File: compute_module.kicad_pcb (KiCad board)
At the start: 4 copper layers, 93.2 x 62.4 mm, 66 parts, among them J1 2001-1-2-21-00-BK, J2 JC-128, P1 POWER, P2 HOST, P3 CAM1, P4 CONN_02X20, Q1 2N7002P.215, Q2 DMP3056L-7, Q3 2N7002P.215, U1 REG1117-3.3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

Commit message: migrate pcb
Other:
- net class Default removed

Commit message: migrate symbols, update footprints
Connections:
- D2 pad 2: Net-(D2-Pad2) -> unconnected-(D2-A-Pad2)
- D3 pad 2: Net-(D3-Pad2) -> unconnected-(D3-A-Pad2)
- D5 pad 3: HDMI_SCL -> Net-(D5-common)
- D6 pad 3: HDMI_SDA -> Net-(D6-common)
- J1 pad 14: Net-(J1-Pad14) -> unconnected-(J1-~-Pad14)
- J2 pad 3: Net-(J2-Pad3) -> unconnected-(J2-TN-Pad3)
- J2 pad 4: Net-(J2-Pad4) -> unconnected-(J2-TR-Pad4)
- MD1 pad 10: Net-(MD1-Pad10) -> unconnected-(MD1G-NC-Pad10)
- MD1 pad 100: Net-(MD1-Pad100) -> unconnected-(MD1E-DSI1_CP-Pad100)
- MD1 pad 101: Net-(MD1-Pad101) -> unconnected-(MD1E-DSI0_DP0-Pad101)
- MD1 pad 102: Net-(MD1-Pad102) -> unconnected-(MD1E-DSI1_CN-Pad102)
- MD1 pad 105: Net-(MD1-Pad105) -> unconnected-(MD1E-DSI0_CN-Pad105)
- MD1 pad 106: Net-(MD1-Pad106) -> unconnected-(MD1E-DSI1_DP3-Pad106)
- MD1 pad 107: Net-(MD1-Pad107) -> unconnected-(MD1E-DSI0_CP-Pad107)
- MD1 pad 108: Net-(MD1-Pad108) -> unconnected-(MD1E-DSI1_DN3-Pad108)
- MD1 pad 112: Net-(MD1-Pad112) -> unconnected-(MD1E-DSI1_DP2-Pad112)
- MD1 pad 114: Net-(MD1-Pad114) -> unconnected-(MD1E-DSI1_DN2-Pad114)
- MD1 pad 118: Net-(MD1-Pad118) -> unconnected-(MD1E-DSI1_DP1-Pad118)
- MD1 pad 12: Net-(MD1-Pad12) -> unconnected-(MD1G-NC-Pad12)
- MD1 pad 120: Net-(MD1-Pad120) -> unconnected-(MD1E-DSI1_DN1-Pad120)
- MD1 pad 124: Net-(MD1-Pad124) -> unconnected-(MD1G-NC-Pad124)
- MD1 pad 126: Net-(MD1-Pad126) -> unconnected-(MD1G-NC-Pad126)
- MD1 pad 128: Net-(MD1-Pad128) -> unconnected-(MD1G-NC-Pad128)
- MD1 pad 130: Net-(MD1-Pad130) -> unconnected-(MD1G-NC-Pad130)
- MD1 pad 132: Net-(MD1-Pad132) -> unconnected-(MD1G-NC-Pad132)
- MD1 pad 136: Net-(MD1-Pad136) -> unconnected-(MD1C-CAM0_DP0-Pad136)
- MD1 pad 138: Net-(MD1-Pad138) -> unconnected-(MD1C-CAM0_DN0-Pad138)
- MD1 pad 142: Net-(MD1-Pad142) -> unconnected-(MD1C-CAM0_CP-Pad142)
- MD1 pad 144: Net-(MD1-Pad144) -> unconnected-(MD1C-CAM0_CN-Pad144)
- MD1 pad 148: Net-(MD1-Pad148) -> unconnected-(MD1C-CAM0_DP1-Pad148)
- MD1 pad 150: Net-(MD1-Pad150) -> unconnected-(MD1C-CAM0_DN1-Pad150)
- MD1 pad 154: Net-(MD1-Pad154) -> unconnected-(MD1G-NC-Pad154)
- MD1 pad 156: Net-(MD1-Pad156) -> unconnected-(MD1G-NC-Pad156)
- MD1 pad 158: Net-(MD1-Pad158) -> unconnected-(MD1G-NC-Pad158)
- MD1 pad 16: Net-(MD1-Pad16) -> unconnected-(MD1G-NC-Pad16)
- MD1 pad 160: Net-(MD1-Pad160) -> unconnected-(MD1G-NC-Pad160)
- MD1 pad 162: Net-(MD1-Pad162) -> unconnected-(MD1G-NC-Pad162)
- MD1 pad 166: Net-(MD1-Pad166) -> unconnected-(MD1G-TVDAC-Pad166)
- MD1 pad 172: Net-(MD1-Pad172) -> unconnected-(MD1G-VC_TRST_N-Pad172)
- MD1 pad 174: Net-(MD1-Pad174) -> unconnected-(MD1G-VC_TDI-Pad174)
- MD1 pad 176: Net-(MD1-Pad176) -> unconnected-(MD1G-VC_TMS-Pad176)
- MD1 pad 177: Net-(MD1-Pad177) -> unconnected-(MD1A-RUN-Pad177)
- MD1 pad 178: Net-(MD1-Pad178) -> unconnected-(MD1G-VC_TDO-Pad178)
- MD1 pad 179: Net-(MD1-Pad179) -> unconnected-(MD1A-VDD_CORE-Pad179)
- MD1 pad 18: Net-(MD1-Pad18) -> unconnected-(MD1G-NC-Pad18)
- MD1 pad 180: Net-(MD1-Pad180) -> unconnected-(MD1G-VC_TCK-Pad180)
- MD1 pad 2: Net-(MD1-Pad2) -> unconnected-(MD1A-EMMC_DISABLE_N-Pad2)
- MD1 pad 22: Net-(MD1-Pad22) -> unconnected-(MD1G-NC-Pad22)
- MD1 pad 24: Net-(MD1-Pad24) -> unconnected-(MD1G-NC-Pad24)
- MD1 pad 4: Net-(MD1-Pad4) -> unconnected-(MD1G-NC-Pad4)
- MD1 pad 46: Net-(MD1-Pad46) -> unconnected-(MD1F-GPIO32-Pad46)
- MD1 pad 48: Net-(MD1-Pad48) -> unconnected-(MD1F-GPIO33-Pad48)
- MD1 pad 52: Net-(MD1-Pad52) -> unconnected-(MD1F-GPIO34-Pad52)
- MD1 pad 54: Net-(MD1-Pad54) -> unconnected-(MD1F-GPIO35-Pad54)
- MD1 pad 58: Net-(MD1-Pad58) -> unconnected-(MD1F-GPIO36-Pad58)
- MD1 pad 6: Net-(MD1-Pad6) -> unconnected-(MD1G-NC-Pad6)
- MD1 pad 60: Net-(MD1-Pad60) -> unconnected-(MD1F-GPIO37-Pad60)
- MD1 pad 64: Net-(MD1-Pad64) -> unconnected-(MD1F-GPIO38-Pad64)
- MD1 pad 66: Net-(MD1-Pad66) -> unconnected-(MD1F-GPIO39-Pad66)
- MD1 pad 72: Net-(MD1-Pad72) -> unconnected-(MD1F-GPIO41-Pad72)
- MD1 pad 76: Net-(MD1-Pad76) -> unconnected-(MD1F-GPIO42-Pad76)
- MD1 pad 78: Net-(MD1-Pad78) -> unconnected-(MD1F-GPIO43-Pad78)
- MD1 pad 93: Net-(MD1-Pad93) -> unconnected-(MD1E-DSI0_DN1-Pad93)
- MD1 pad 94: Net-(MD1-Pad94) -> unconnected-(MD1E-DSI1_DP0-Pad94)
- MD1 pad 95: Net-(MD1-Pad95) -> unconnected-(MD1E-DSI0_DP1-Pad95)
- MD1 pad 96: Net-(MD1-Pad96) -> unconnected-(MD1E-DSI1_DN0-Pad96)
- MD1 pad 99: Net-(MD1-Pad99) -> unconnected-(MD1E-DSI0_DN0-Pad99)
- P1 pad 2: Net-(P1-Pad2) -> unconnected-(P1-D--Pad2)
- P1 pad 3: Net-(P1-Pad3) -> unconnected-(P1-D+-Pad3)
- P1 pad 4: Net-(P1-Pad4) -> unconnected-(P1-ID-Pad4)
- Q2 pad 2: +5V -> Net-(Q2-S)
- R4 pad 2: HDMI_SCL -> Net-(D5-common)
- R5 pad 2: HDMI_SDA -> Net-(D6-common)

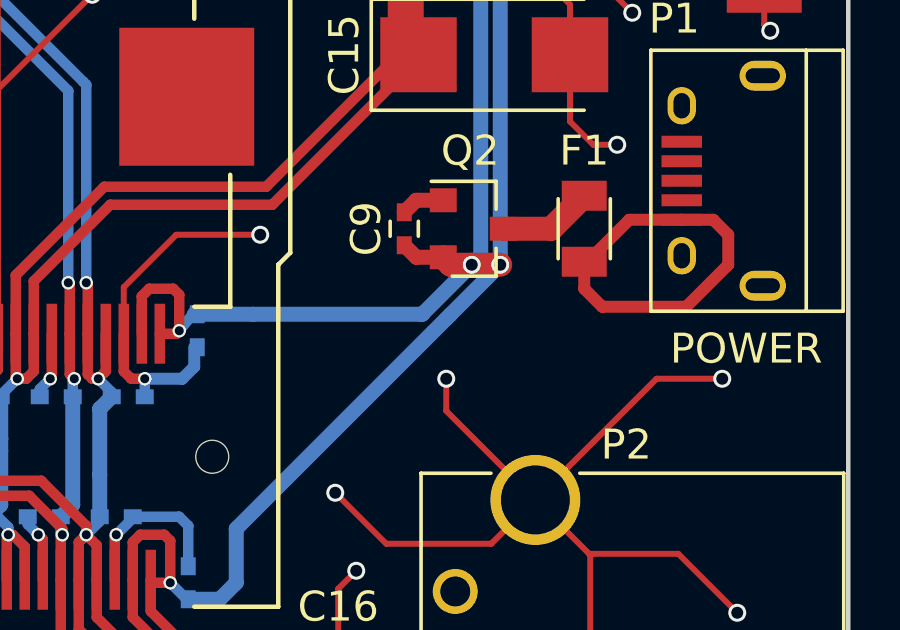
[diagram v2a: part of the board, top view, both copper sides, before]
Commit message: fix missing hdmi junctions, dangling trace
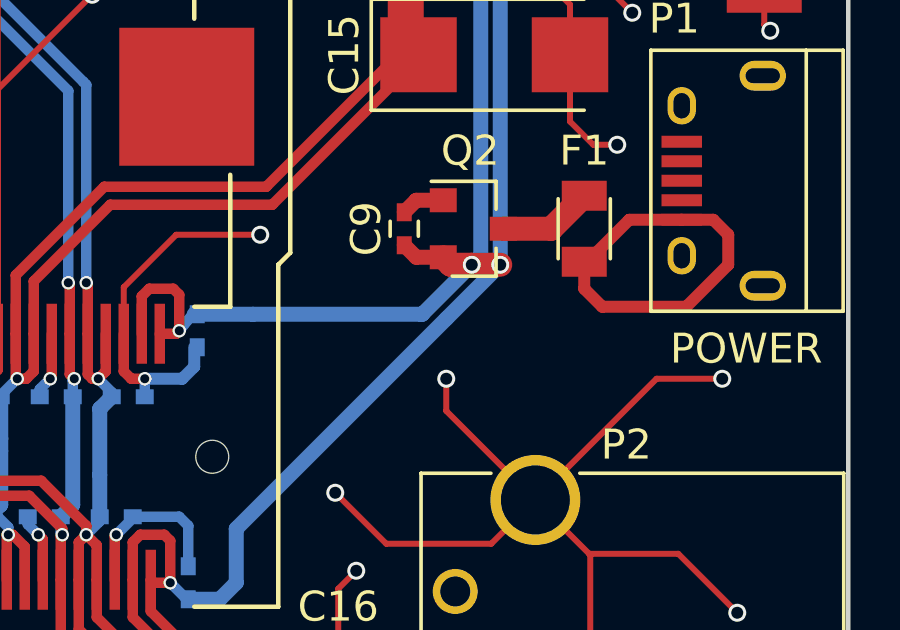
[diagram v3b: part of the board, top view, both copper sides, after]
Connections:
- D5 pad 3: Net-(D5-common) -> HDMI_SCL
- D6 pad 3: Net-(D6-common) -> HDMI_SDA
- Q2 pad 2: Net-(Q2-S) -> +5V
- R4 pad 2: Net-(D5-common) -> HDMI_SCL
- R5 pad 2: Net-(D6-common) -> HDMI_SDA
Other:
- rule pad_to_mask_clearance: 0.2 -> 0.05
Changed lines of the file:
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@@
 	)
 	(setup
-		(pad_to_mask_clearance 0.2)
+		(stackup
+			(layer "F.SilkS"
+				(type "Top Silk Screen")
+			)
+			(layer "F.Paste"
+				(type "Top Solder Paste")
+			)
+			(layer "F.Mask"
+				(type "Top Solder Mask")
+				(thickness 0.01)
+			)
+			(layer "F.Cu"
+				(type "copper")
+				(thickness 0.035)
+			)
+			(layer "dielectric 1"
+				(type "core")
+				(thickness 0.48)
+				(material "FR4")
+				(epsilon_r 4.5)
+				(loss_tangent 0.02)
+			)
+			(layer "In1.Cu"
+				(type "copper")
+				(thickness 0.035)
+			)
+			(layer "dielectric 2"
+				(type "prepreg")
+				(thickness 0.48)
+				(material "FR4")
+				(epsilon_r 4.5)
+				(loss_tangent 0.02)
+			)
+			(layer "In2.Cu"
+				(type "copper")
+				(thickness 0.035)
+			)
+			(layer "dielectric 3"
+				(type "core")
+				(thickness 0.48)
+				(material "FR4")
+				(epsilon_r 4.5)
+				(loss_tangent 0.02)
+			)
+			(layer "B.Cu"
+				(type "copper")
+				(thickness 0.035)
+			)
+			(layer "B.Mask"
+				(type "Bottom Solder Mask")
+				(thickness 0.01)
+			)
+			(layer "B.Paste"
+				(type "Bottom Solder Paste")
+			)
+			(layer "B.SilkS"
+				(type "Bottom Silk Screen")
+			)
+			(copper_finish "None")
+			(dielectric_constraints no)
+		)
+		(pad_to_mask_clearance 0.05)
 		(allow_soldermask_bridges_in_footprints no)
 		(tenting
@@
 			(size 0.9 0.8)
 			(layers "F.Cu" "F.Mask" "F.Paste")
-			(net "Net-(Q2-S)")
+			(net "+5V")
 			(pinfunction "S_2")
 			(pintype "passive")
@@
 			(size 0.9 0.8)
 			(layers "B.Cu" "B.Mask" "B.Paste")
-			(net "Net-(D5-common)")
+			(net "HDMI_SCL")
 			(pinfunction "common_3")
 			(pintype "passive")
@@
 			(size 0.9 0.8)
 			(layers "B.Cu" "B.Mask" "B.Paste")
-			(net "Net-(D6-common)")
+			(net "HDMI_SDA")
 			(pinfunction "common_3")
 			(pintype "passive")
@@
 			(size 1.2 0.9)
 			(layers "B.Cu" "B.Mask" "B.Paste")
-			(net "Net-(D5-common)")
+			(net "HDMI_SCL")
 			(pinfunction "~_2")
 			(pintype "passive")
@@
 			(size 1.2 0.9)
 			(layers "B.Cu" "B.Mask" "B.Paste")
-			(net "Net-(D6-common)")
+			(net "HDMI_SDA")
 			(pinfunction "~_2")
 			(pintype "passive")
@@
 		(width 0.5)
 		(layer "B.Cu")
-		(net "+5V")
-	)
-	(segment
-		(start 167.55 79.25)
-		(end 167.5 79.3)
-		(width 0.5)
-		(layer "B.Cu")
